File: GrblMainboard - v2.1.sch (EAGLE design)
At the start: 60 parts, among them IC1 LM7805

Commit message: Power wires thicker for ~ 3A
- make power wires thicker
- check for error in DRU schema and board
- replace Atmega328U with Atmega328
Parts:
- C10, C5, C7: value (none) -> 47uF
- JP1, JP2, JP3, JP4: value (none) -> microstep
- JP6: value (none) -> ICSP
- JP8: value (none) -> DualY
- LED1: value (none) -> Data
- Q2: value (none) -> 16 MHZ
- renumbered ATMEGA328U to ATMEGA328
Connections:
- net !RESET1 renamed RESET
- net GND: now also H5.MOUNT, H6.MOUNT, H7.MOUNT, H8.MOUNT
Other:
- moved on the sheet: H5, H6, H7, H8

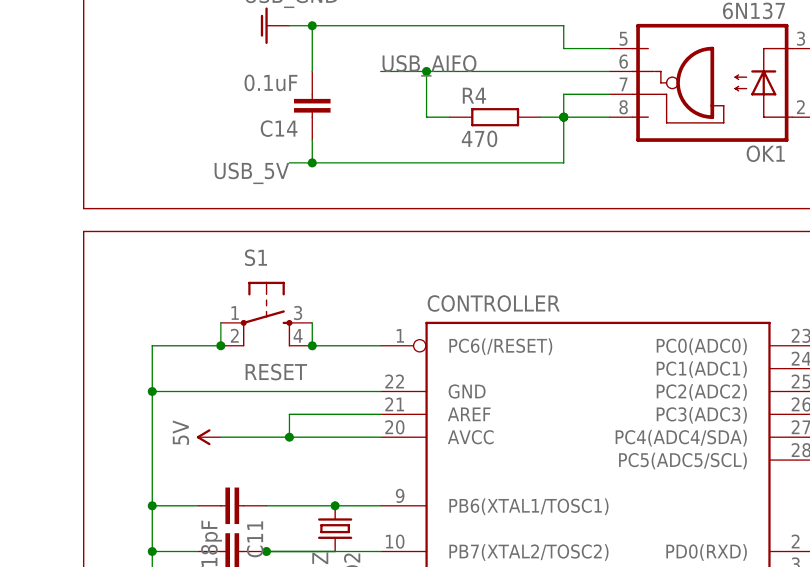
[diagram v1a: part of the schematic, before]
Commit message: Add pullup Resistor for Atmel Reset pin
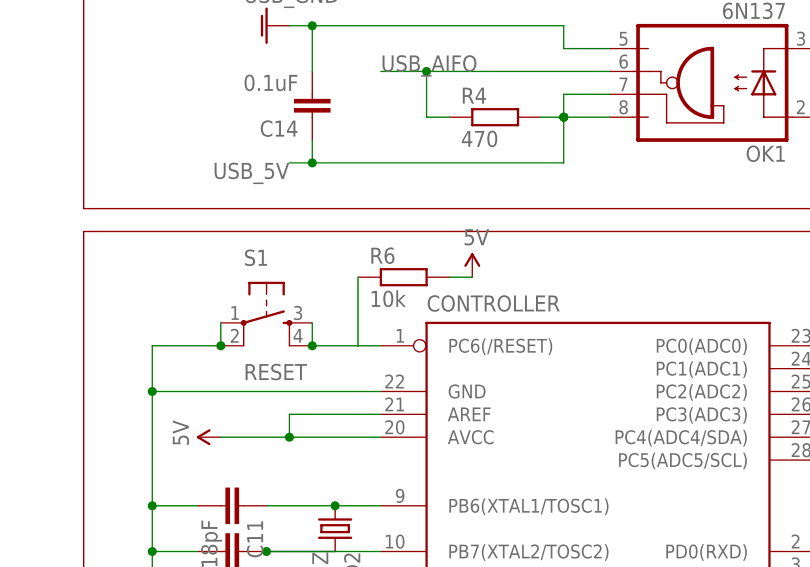
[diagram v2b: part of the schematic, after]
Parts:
- added R6: 10k, resistor:R-EU_0207/10
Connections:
- net 5V: now also R6.2
- net RESET: now also R6.1
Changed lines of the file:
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@@
 <part name="SWT6" library="SparkFun" deviceset="M02" device="5MM" value="SPINDLE-DIR"/>
 <part name="SWT7" library="SparkFun" deviceset="M02" device="5MM" value="SPINDLE-ENABLE"/>
+<part name="R6" library="resistor" deviceset="R-EU_" device="0207/10" value="10k"/>
+<part name="U$15" library="SparkFun" deviceset="5V" device=""/>
 </parts>
 <sheets>
@@
 <instance part="SWT6" gate="G$1" x="307.34" y="162.56" rot="R180"/>
 <instance part="SWT7" gate="G$1" x="307.34" y="177.8" rot="R180"/>
+<instance part="R6" gate="G$1" x="35.56" y="88.9"/>
+<instance part="U$15" gate="G$1" x="43.18" y="88.9"/>
 </instances>
 <busses>
@@
 <pinref part="U$13" gate="G$1" pin="5V"/>
 </segment>
+<segment>
+<pinref part="R6" gate="G$1" pin="2"/>
+<pinref part="U$15" gate="G$1" pin="5V"/>
+<wire x1="40.64" y1="88.9" x2="43.18" y2="88.9" width="0.1524" layer="91"/>
+</segment>
 </net>
 <net name="AIFO" class="0">
@@
 <pinref part="S1" gate="S" pin="3"/>
 <wire x1="25.4" y1="83.82" x2="25.4" y2="81.28" width="0.1524" layer="91"/>
-<wire x1="25.4" y1="81.28" x2="33.02" y2="81.28" width="0.1524" layer="91"/>
-</segment>
-</net>
+<wire x1="25.4" y1="81.28" x2="30.48" y2="81.28" width="0.1524" layer="91"/>
+<pinref part="R6" gate="G$1" pin="1"/>
+<wire x1="30.48" y1="81.28" x2="33.02" y2="81.28" width="0.1524" layer="91"/>
+<wire x1="30.48" y1="81.28" x2="30.48" y2="88.9" width="0.1524" layer="91"/>
+</segment>
+</net>
